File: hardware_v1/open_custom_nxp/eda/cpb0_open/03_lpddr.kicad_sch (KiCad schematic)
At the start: 0 parts

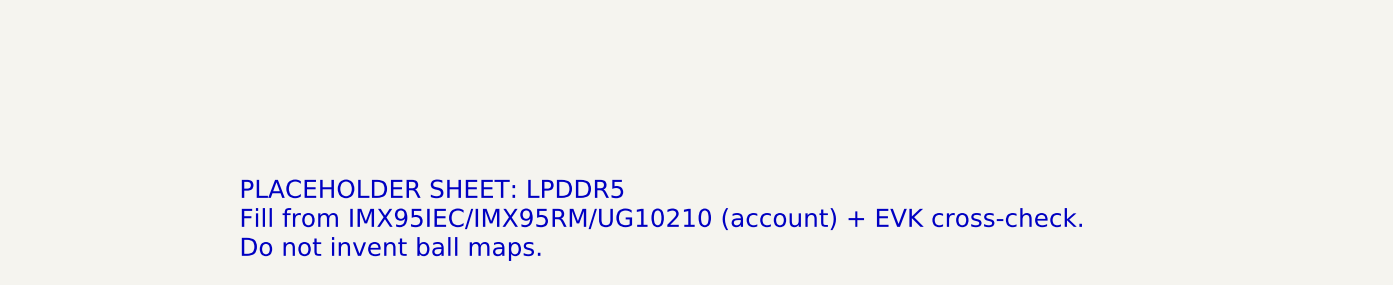
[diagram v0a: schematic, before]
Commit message: feat(nxp): complete CPB0 schematic and ERC
Advance hierarchical sheets with SoC/PMIC/LPDDR design status and honest ERC non-pass reporting; full multi-unit wiring remains open.

Co-authored-by: Cursor <cursoragent@cursor.com>
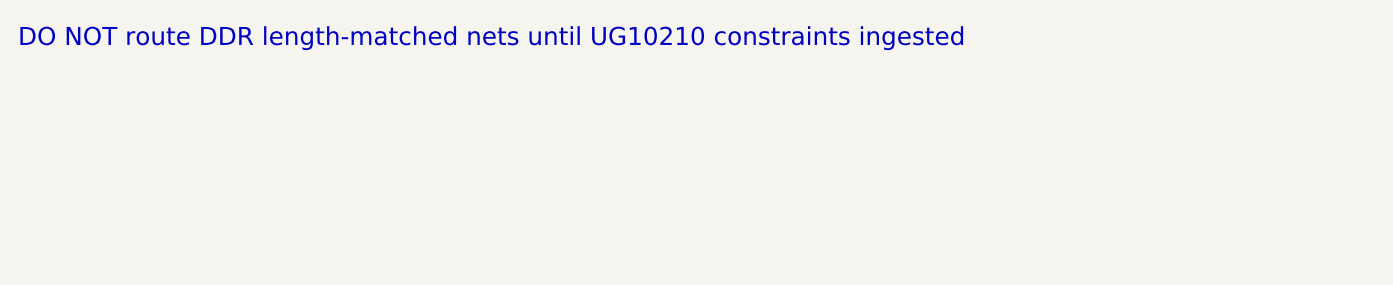
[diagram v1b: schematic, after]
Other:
- note added: "DO NOT route DDR length-matched nets until UG10210 constraints ingested"
- note removed: "PLACEHOLDER SHEET: LPDDR5 Fill from IMX95IEC/IMX95RM/UG10210 (account) + EVK cross-check. Do not invent ball maps."
- company: gunnchOS3k / NXP-0 -> (none)
- title: CPB0-O / LPDDR5 -> 03 LPDDR5 x32
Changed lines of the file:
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@@
-(kicad_sch (version 20250114) (generator "nxp0_campaign") (generator_version "10.0")
+(kicad_sch
+  (version 20231120)
+  (generator "nxp1")
   (paper "A3")
-  (title_block
-    (title "CPB0-O / LPDDR5")
-    (date "2026-09-18")
-    (rev "0.0.1-nxp0")
-    (company "gunnchOS3k / NXP-0")
-    (comment 1 "PLACEHOLDER — not symbol-complete")
-    (comment 2 "Public-collateral only; no NDA")
-    (comment 3 "CPB0_OPEN_READY_FOR_FAB=false")
-  )
-  (text "PLACEHOLDER SHEET: LPDDR5\nFill from IMX95IEC/IMX95RM/UG10210 (account) + EVK cross-check.\nDo not invent ball maps."
-    (exclude_from_sim no) (at 50 50 0)
-    (effects (font (size 2 2)) (justify left bottom))
-  )
-  (sheet_instances
-    (path "/" (page "1"))
-  )
+  (title_block (title "03 LPDDR5 x32") (date "2026-09-18") (rev "NXP1")
+    (comment 1 "SoC DRAM_* balls assigned; device MPN + length rules BLOCKED on UG10210/EVK BOM"))
+  (text "DO NOT route DDR length-matched nets until UG10210 constraints ingested"
+    (exclude_from_sim no) (at 25.4 25.4 0) (effects (font (size 2 2)) (justify left))
 )
+  (sheet_instances ((path "/" (page "4"))))
+)
